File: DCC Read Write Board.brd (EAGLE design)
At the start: 93.2 x 67 mm, 159 parts, among them IC5 4163D, J103 686318124422, J111 PTR1PAD1-17, J112 PTR1PAD1-17, J121 PTR1PAD1-17, J122 PTR1PAD1-17, K1 68613014122, Q101 TDA1317, Q102 2SC2712GR, Q103 2SC2712GR, Q104 2SD99CL, Q105 BCX71SMD, Q106 2SC2712GR, Q151 TDA1316, Q153 MUN2211T1, Q180 2SC2712GR, Q181 744053D, Q182 74HCT175D, Q183 74HC00D, Q190 2SC2712GR, U185 74HC02D

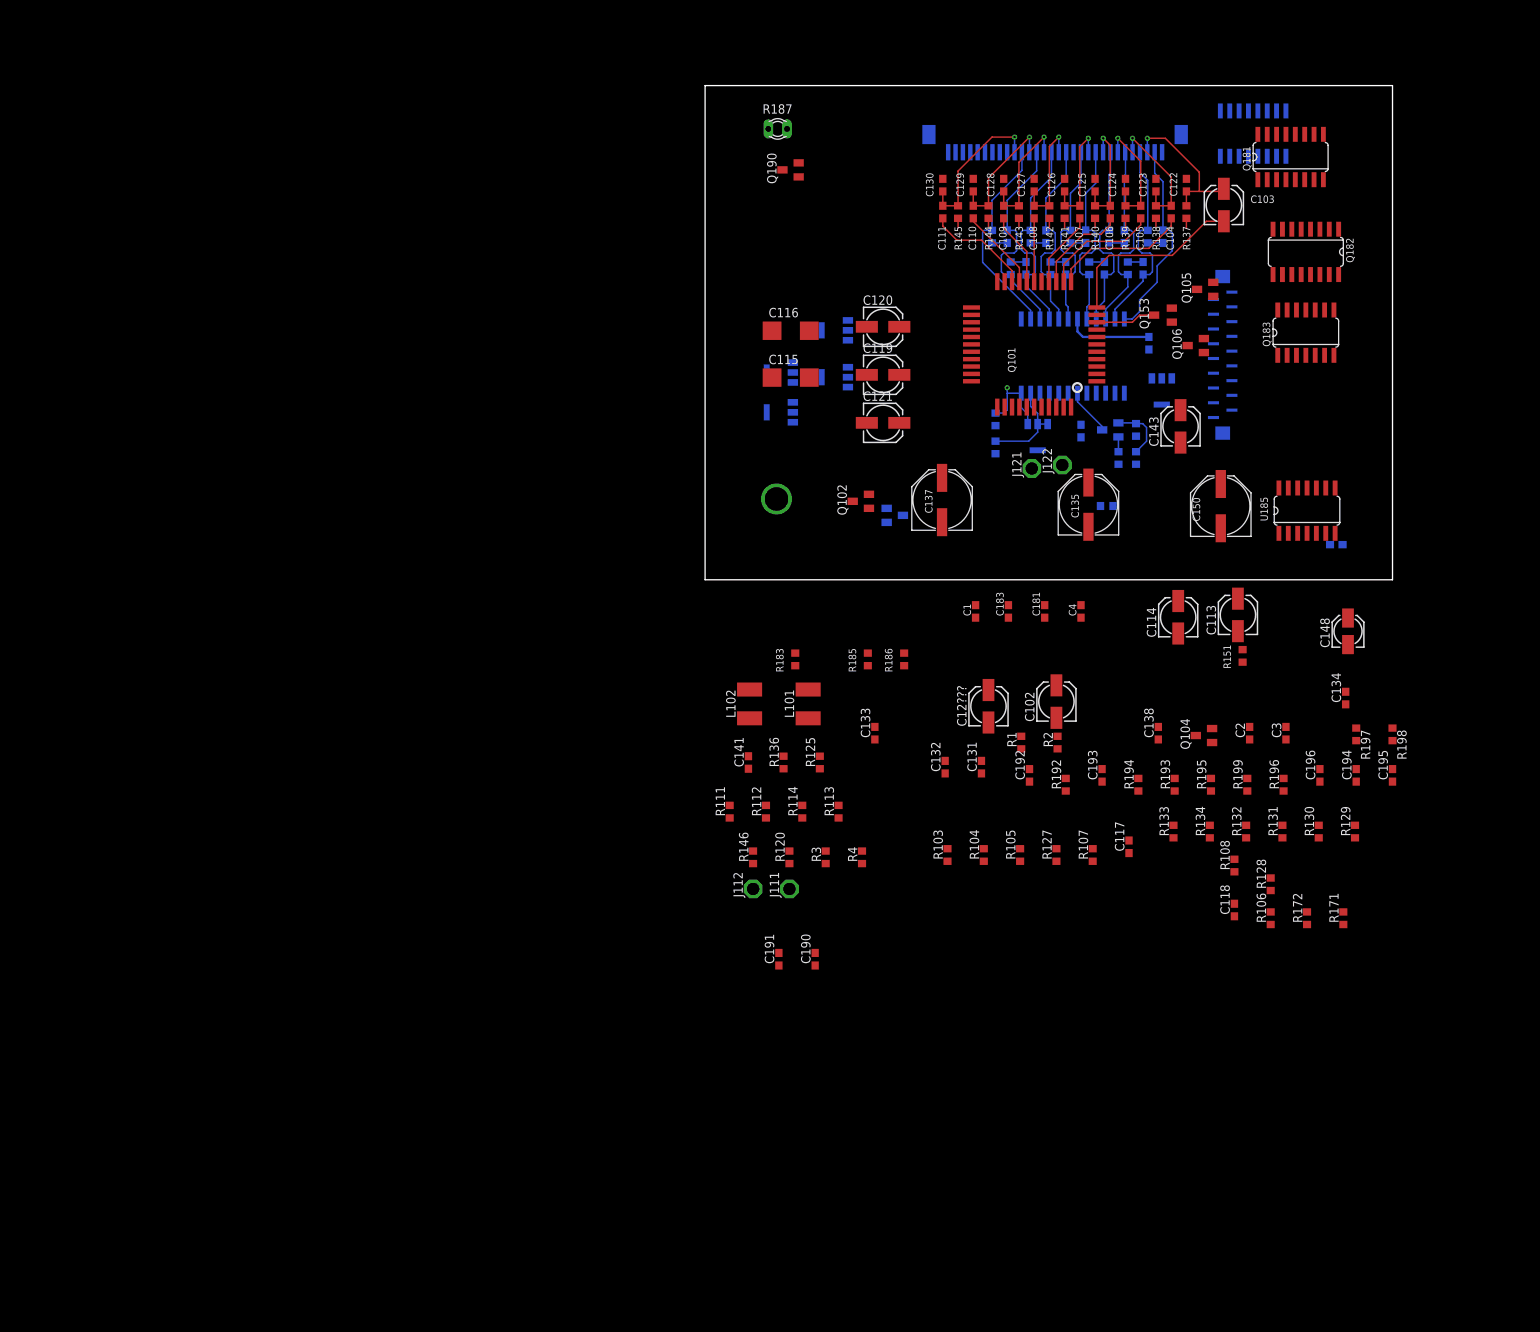
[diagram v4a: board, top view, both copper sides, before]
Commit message: Initial parts placement done
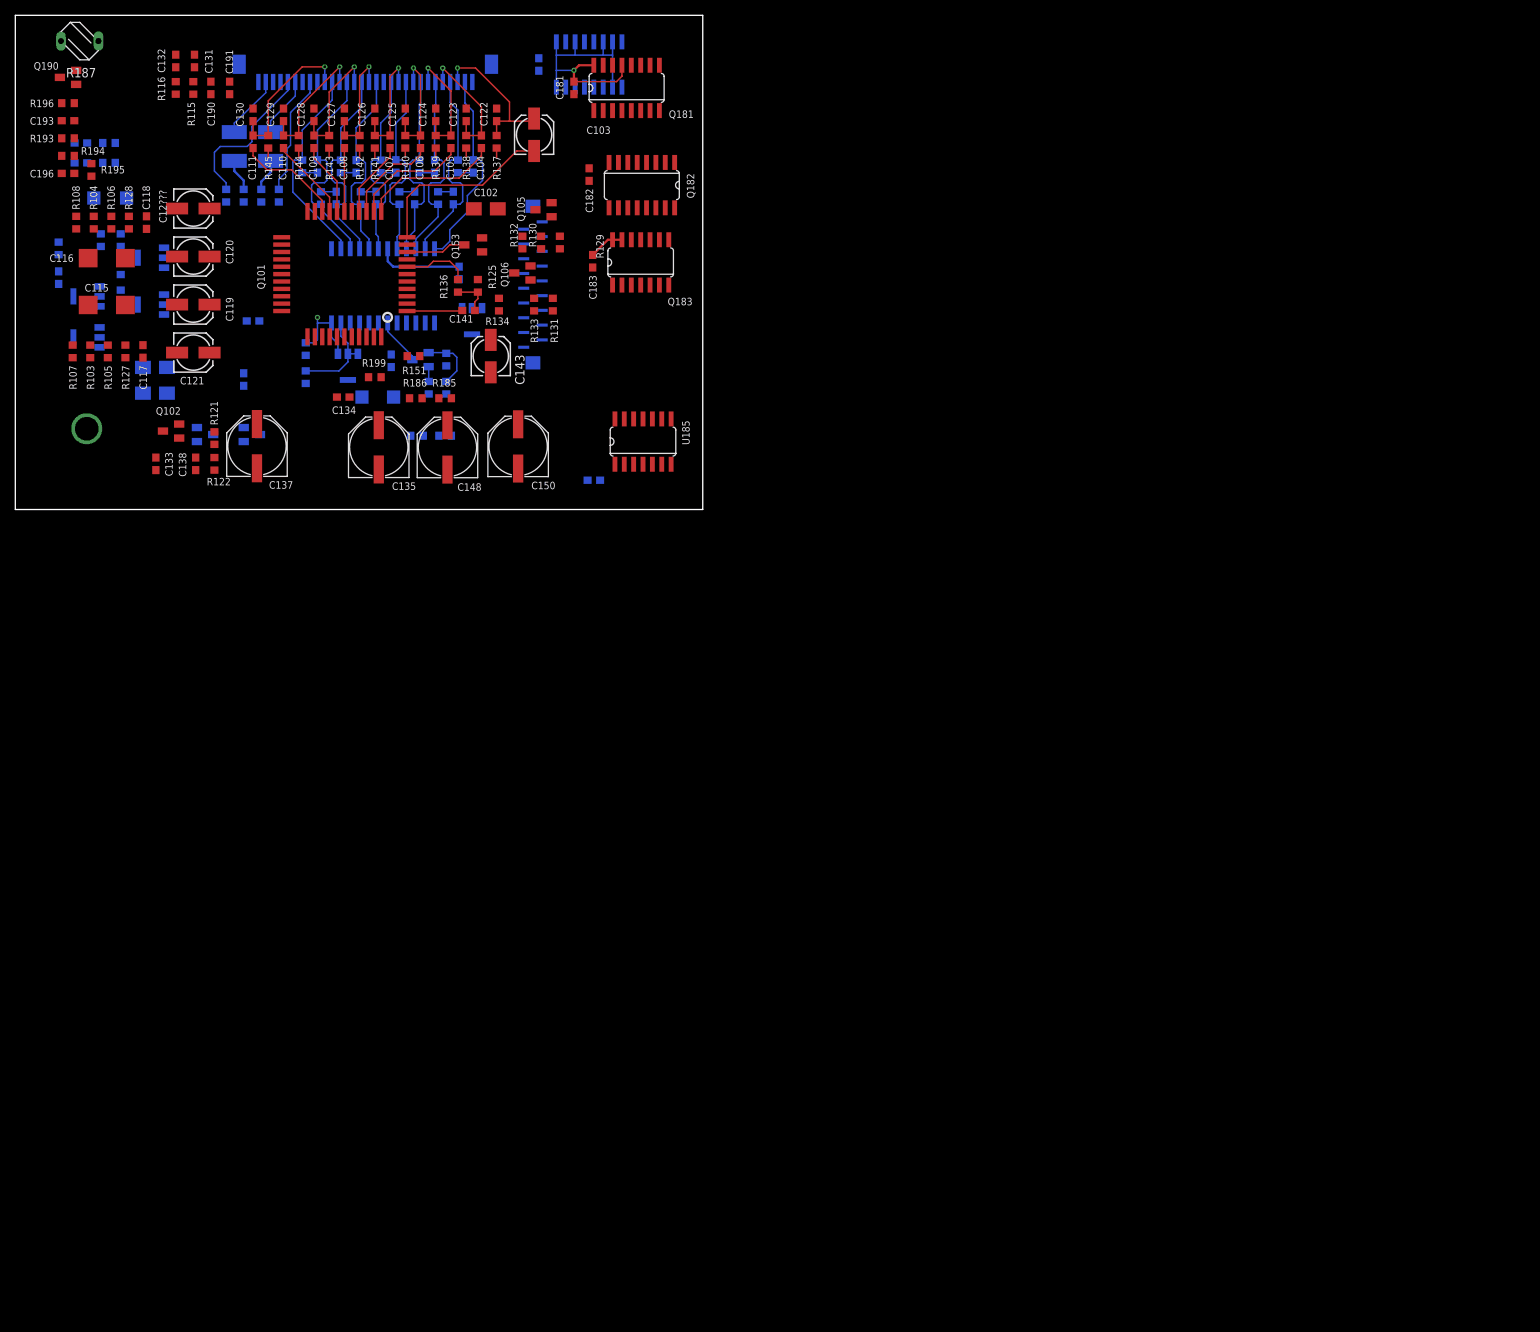
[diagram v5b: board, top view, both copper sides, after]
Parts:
- removed C1, C4: 100nF, rcl:C0603
- removed C2, C3: 1uF, rcl:C0603
- removed IC5: 4163D, 40xx:SO16
- removed K1: 68613014122, FPC_Connectors_Flat_Flexible_Cable_rev15c:68613014122
- removed R1, R2, R3, R4: 560R, rcl:R0603
- added C144, C145: 1uF, rcl:C0603
- added C182, C184: 100nF, rcl:C0603
- added J101: 68613014122, FPC_Connectors_Flat_Flexible_Cable_rev15c:68613014122
- added Q184: 4163D, 40xx:SO16
- added R115, R116: 560R, rcl:R0603
- added R121: 6K8, rcl:R0603
- added R122: 68K, rcl:R0603
- C102, C113, C114: device rcl:153CLV-0505 -> rcl:B/3528-21W
- C148: device rcl:153CLV-0405 -> rcl:PANASONIC_E
- J111, J112, J121, J122: value PTR1PAD1-17 -> PTR1TP18SQ; device testpad:P1-17 -> testpad:TP18SQ
- R187: device ptc-ntc:P640 -> ptc-ntc:B57164
- moved C195 197.4 mm to (-88.4, 53.2), flipped to the bottom, turned to 180 degrees
- moved C194 191.8 mm to (-88.4, 50.5), flipped to the bottom, turned to 180 degrees
- moved R198 191.6 mm to (-84.6, 53.2), flipped to the bottom, turned to 0 degrees
- moved R196 188.9 mm to (-90.2, 58.6), turned to 0 degrees
- moved C196 188.3 mm to (-90.2, 49.1), turned to 0 degrees
- moved R197 186.0 mm to (-84.6, 50.5), flipped to the bottom, turned to 180 degrees
- moved R171 185.9 mm to (-83.0, 32.4), flipped to the bottom, turned to 270 degrees
- moved R172 183.4 mm to (-83.0, 36.2), flipped to the bottom
- moved R106 183.3 mm to (-84.3, 42.4)
- moved R108 179.6 mm to (-89.1, 42.4)
- moved R128 178.9 mm to (-81.9, 42.4), turned to 270 degrees
- moved C118 174.5 mm to (-79.5, 42.4), turned to 270 degrees
- moved R193 173.7 mm to (-90.2, 53.8), turned to 0 degrees
- moved R195 173.1 mm to (-87.0, 49.5)
- moved R194 168.3 mm to (-90.2, 51.4), turned to 180 degrees
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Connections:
- net +5V_WRITE: now also C182.1, C184.1, Q184.1, Q184.10, Q184.16, Q184.3, Q184.6, Q184.7; no longer C1.1, C4.1, IC5.1, IC5.10, IC5.16, IC5.3, IC5.6, IC5.7
- net +8V: now also R121.2; no longer R1.2
- net BIAS1: now also J101.9; no longer K1.9
- net GND: now also C144.2, C145.2, C182.2, C184.2, J101.18, J101.3, J101.30, Q184.4, Q184.5, Q184.8, R122.1; no longer C1.2, C2.2, C3.2, C4.2, IC5.4, IC5.5, IC5.8, K1.18, K1.3, K1.30, R2.1
- net IRH0: now also J101.29; no longer K1.29
- net IRH1: now also J101.27; no longer K1.27
- net IRH2: now also J101.25; no longer K1.25
- net IRH3: now also J101.23; no longer K1.23
- net IRH4: now also J101.21; no longer K1.21
- net IRH5: now also J101.19; no longer K1.19
- net IRH6: now also J101.17; no longer K1.17
- net IRH7: now also J101.15; no longer K1.15
- net IRH8: now also J101.13; no longer K1.13
- net IRH9: now also J101.11; no longer K1.11
- net MFL_A: now also J101.5
- net MFL_B: now also J101.2
- net MFR_A: now also J101.8
- net MFR_B: now also J101.6
- net MRH_L: now also J101.4, R115.1; no longer K1.4, R4.1
- net MRH_R: now also J101.7, R116.1; no longer K1.7, R3.1
- net N$11: now also Q184.9; no longer IC5.9
- net N$13: now also Q184.15; no longer IC5.15
- net N$19: now also J101.10; no longer K1.10
- net N$20: now also J101.12; no longer K1.12
- net N$21: now also J101.14; no longer K1.14
- net N$22: now also J101.16; no longer K1.16
- net N$23: now also J101.20; no longer K1.20
- net N$24: now also J101.22; no longer K1.22
- net N$25: now also J101.24; no longer K1.24
- net N$26: now also J101.26; no longer K1.26
- net N$27: now also J101.28; no longer K1.28
- net N$52: now also R121.1, R122.2; no longer R1.1, R2.2
- net VSENSE_1: now also C144.1; no longer C2.1
- net VSENSE_2: now also C145.1, R115.2, R116.2; no longer C3.1, R3.2, R4.2
- net WCLCK: now also Q184.2; no longer IC5.2
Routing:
- net +5V_WRITE: track 11.7 -> 55.2 mm, vias 0 -> 1
- net MFL_A: track 0.00 -> 21.5 mm
- net MFR_A: track 0.00 -> 16.3 mm
- net N$55: track 0.00 -> 9.04 mm
- net MFL_B: track 0.00 -> 8.61 mm
- net MFR_B: track 0.00 -> 8.18 mm
- net N$54: track 0.00 -> 7.51 mm
- net N$56: track 0.00 -> 5.36 mm
- net N$66: track 0.00 -> 4.39 mm
- net N$67: track 0.00 -> 4.39 mm
